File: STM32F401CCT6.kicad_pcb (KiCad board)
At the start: 2 copper layers, 52 x 23 mm, 43 parts, among them J1 USB_OTG, J2 Conn_02x03_Odd_Even, J3 Conn_01x20_des, J4 Conn_01x05_desc, J5 Conn_01x20, SW1 SW_Push, U1 MIC5219-3.3, U2 STM32F401CCT6, U3 USBLC6-2SC6, Y1 32.786K, Y2 8MHz

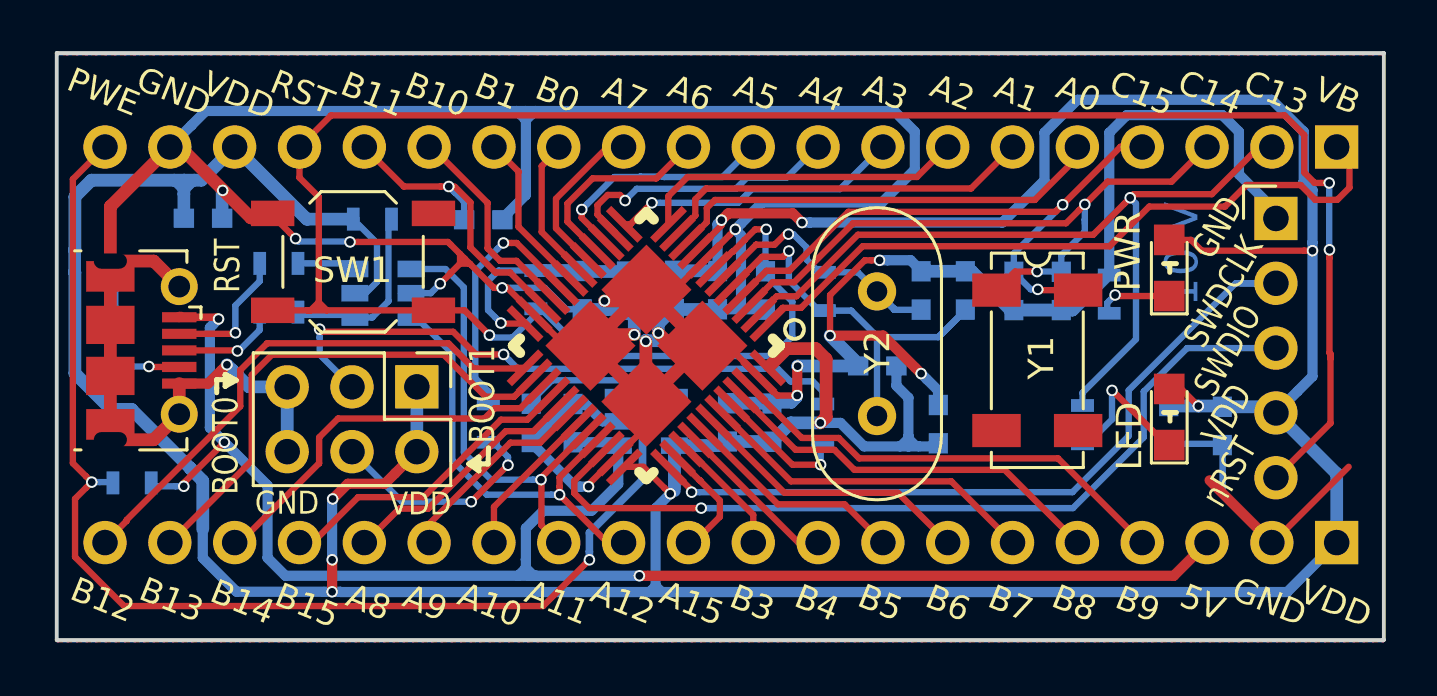
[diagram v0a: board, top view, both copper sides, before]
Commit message: Replace the Micro-USB footprint with the one newly created, added a shield for MCU (grounded pin), moved some component inwards to prevent touching the pinheader plastic.
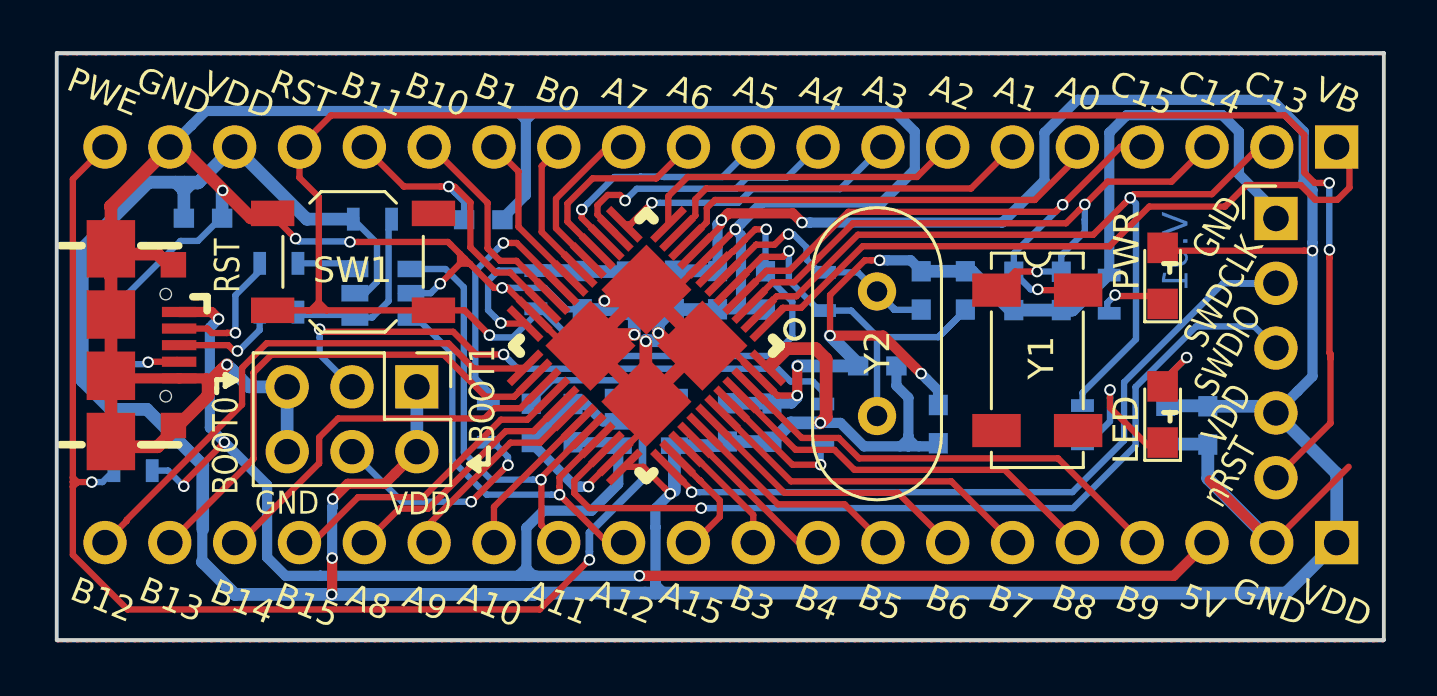
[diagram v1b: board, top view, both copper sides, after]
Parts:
- removed LED, PWR: LED_ALT, LEDs:LED_0805
- added D1: RED_LED, LEDs:LED_0805, F.Cu at (79.9, 57.9)
- added D2: BLUE_LED, LEDs:LED_0805, F.Cu at (79.9, 63.3)
- J1: footprint Connectors_USB:USB_Micro-B_Molex-105017-0001 -> MicroUSB(SMD)
- moved J1 1.32 mm to (40.3, 60.6), turned to 90 degrees
- moved C17 0.57 mm to (81.7, 63.8)
- moved R11 0.48 mm to (39.6, 65.5)
- moved R9 0.15 mm to (38.8, 60.6)
- moved C14 0.12 mm to (80.0, 63.7)
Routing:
- net GND: track 227.5 -> 235.2 mm
- net /PWR_EN: track 47.9 -> 48.9 mm
- net /SWDIO: track 33.6 -> 34.6 mm
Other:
- board text added: "LED"
- board text added: "PWR"

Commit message: Moved the indicator of LED slightly to the right
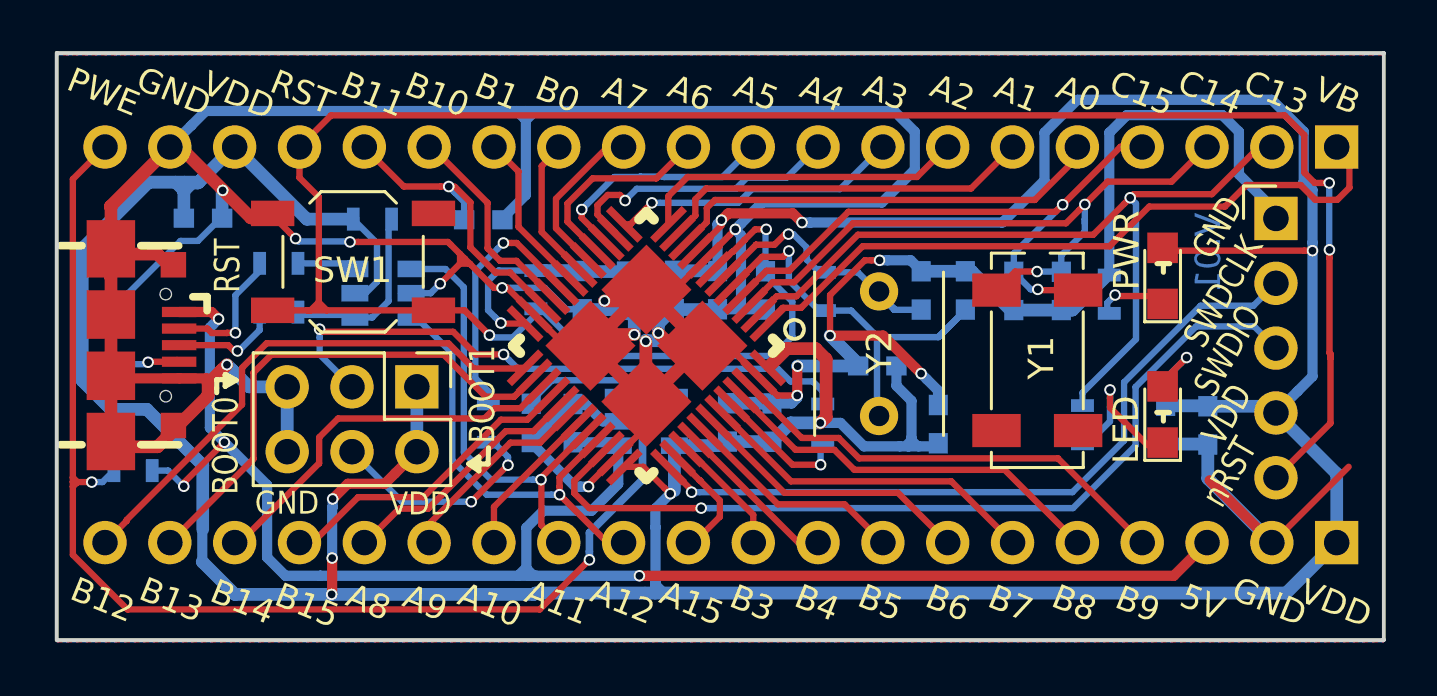
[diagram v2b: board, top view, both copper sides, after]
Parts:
- moved Y2 0.08 mm to (68.8, 63.4)
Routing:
- net /SWDCLK: track 30.4 -> 29.0 mm

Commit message: Replaced the MCU footprint
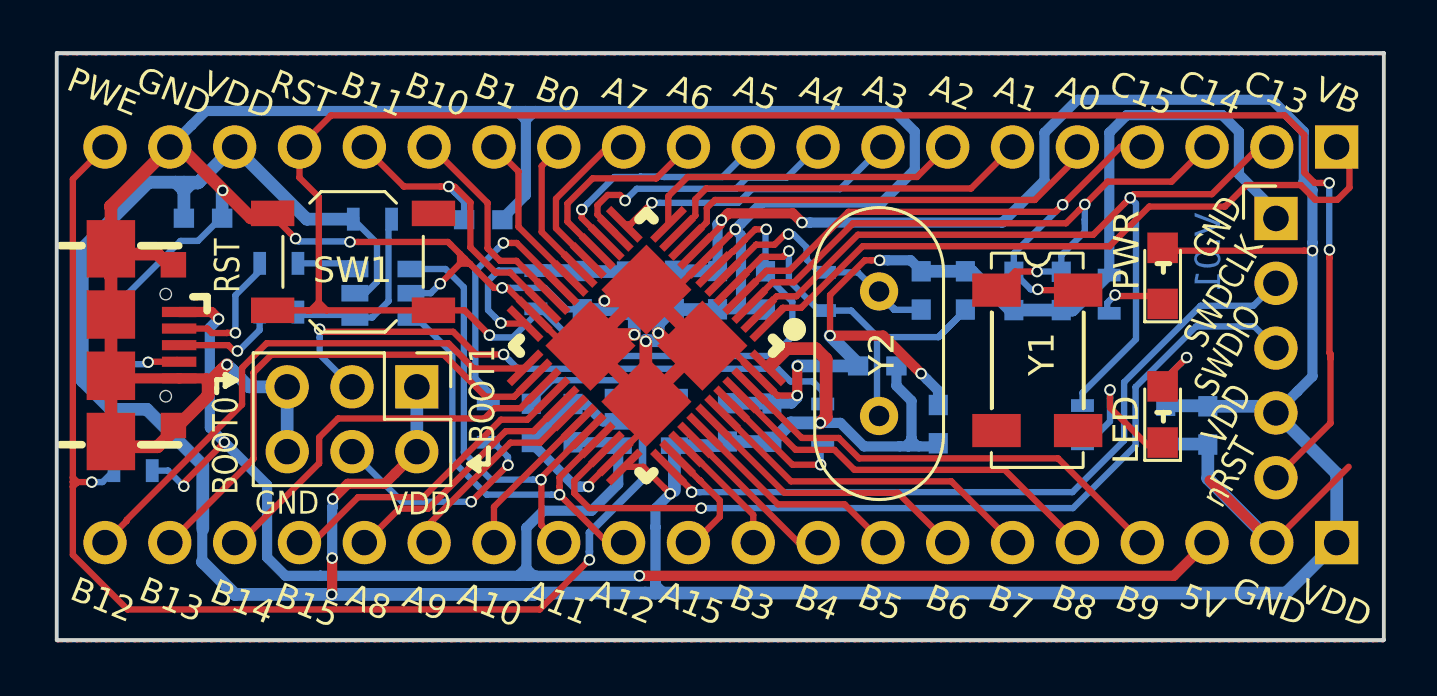
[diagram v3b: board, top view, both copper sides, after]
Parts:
- added Dot: G***, crystal:Dot, F.Cu at (65.5, 60.0)
- added HS_Crystal: G***, crystal:HS_Crystal, F.Cu at (68.8, 60.9)
- added LS_Crystal: G***, crystal:LS_Crystal, F.Cu at (75.0, 61.2)

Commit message: Changed the kitty silk layer
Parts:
- added Meow: G***, crystal:Meow, B.Cu at (74.0, 63.0)
